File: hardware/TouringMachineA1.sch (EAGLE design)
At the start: 62 parts, among them IC1 78L05F, J1 PJ301_THONKICONN6, J2 PJ301_THONKICONN6, J3 PJ301_THONKICONN6, J4 PJ301_THONKICONN6, U1 MCP6002_, U2 TL072_SMD

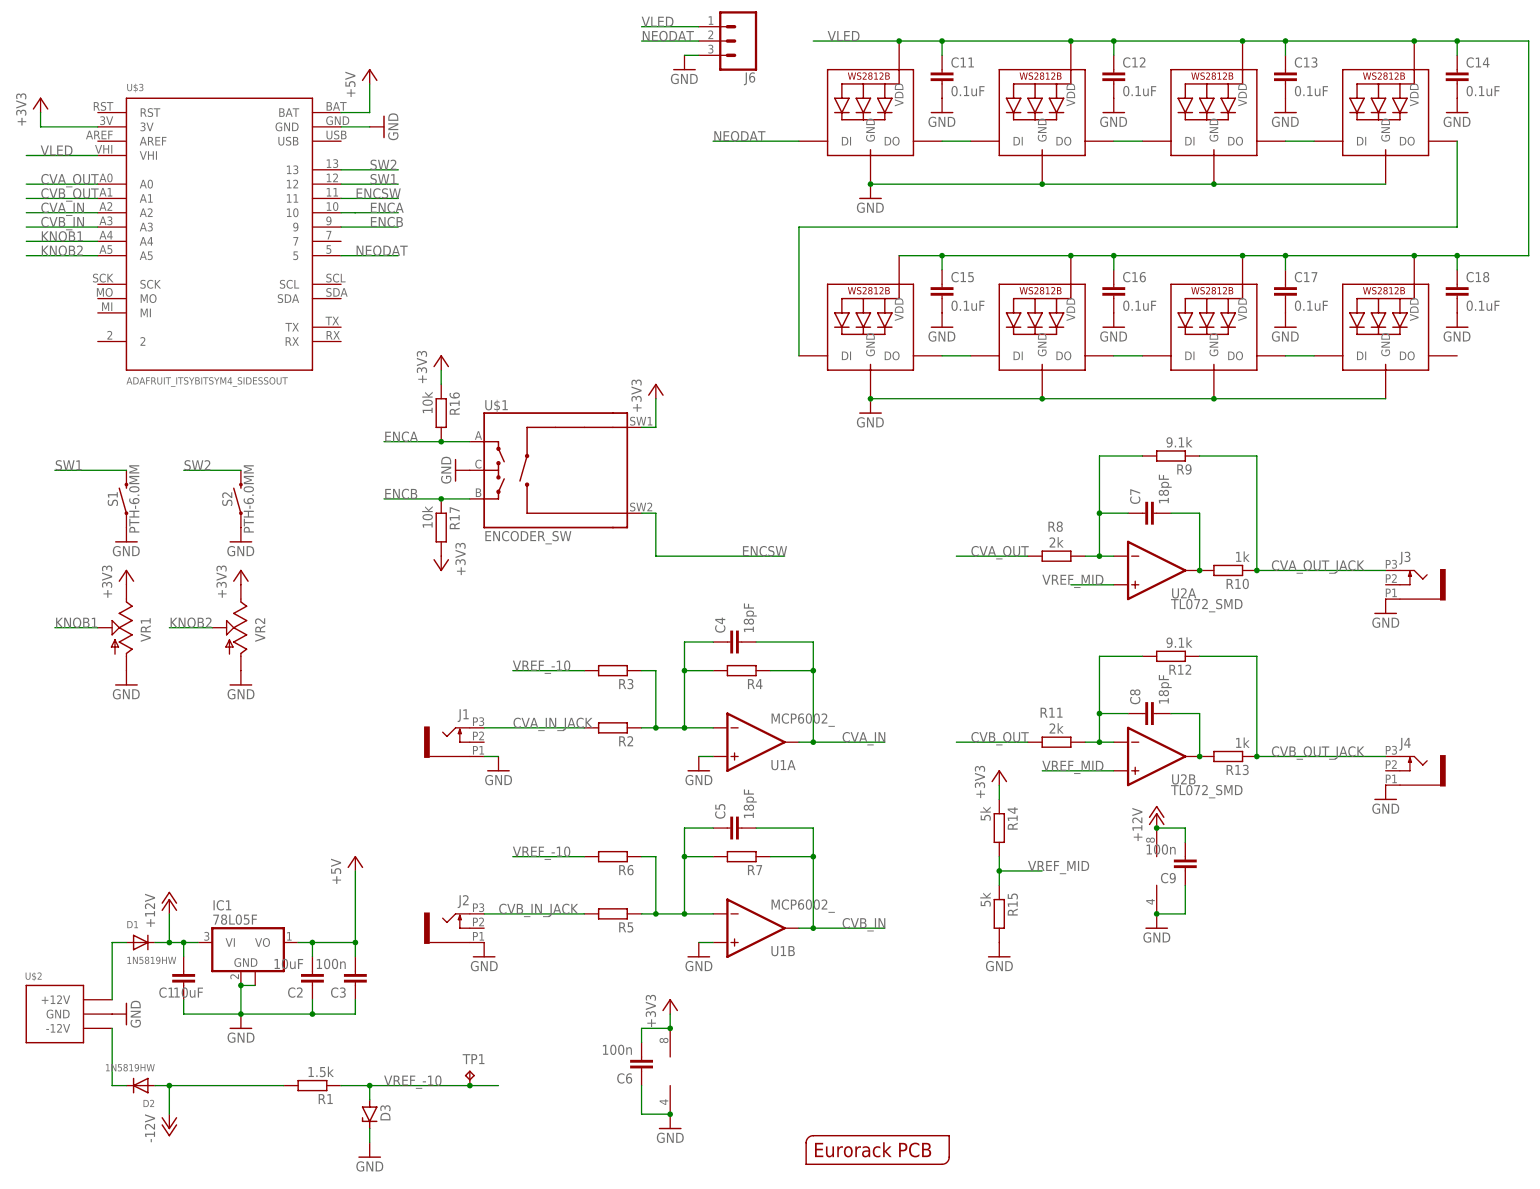
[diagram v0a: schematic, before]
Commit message: added 3d models
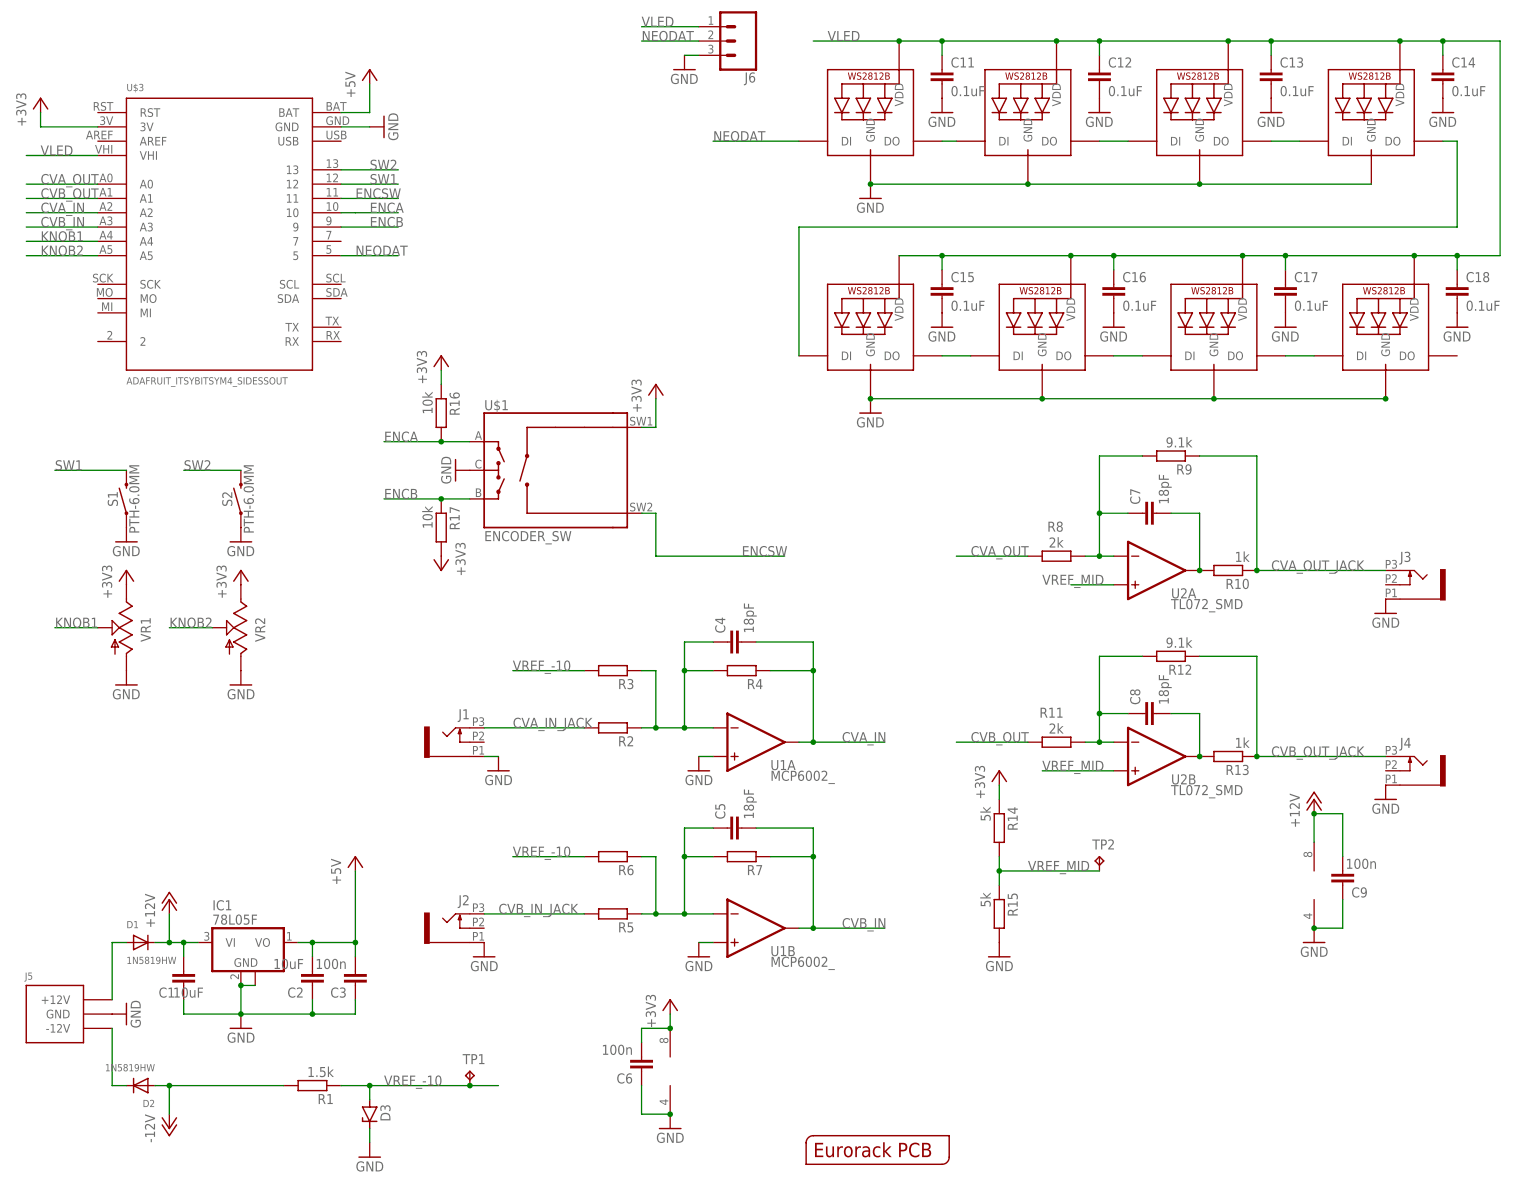
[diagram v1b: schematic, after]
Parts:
- added TP2: TPTP15R, testpad:TPTP15R
- renumbered U$2 to J5
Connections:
- net VREF_MID: now also TP2.TP
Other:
- moved on the sheet: C12, C13, C14, C9
